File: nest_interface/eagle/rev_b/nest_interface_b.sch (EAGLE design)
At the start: 141 parts, among them J1 MOLEX_MICRO_USB_B_047346, J10 CONN_BLOCK_2, J11 CONN_BLOCK_2, J12 CONN_BLOCK_2, J13 CONN_BLOCK_2, J14 CONN_BLOCK_3, J15 CONN_BLOCK_3, J16 CONN_BLOCK_7, J17 CONN_BLOCK_7, J18 CONN_BLOCK_8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

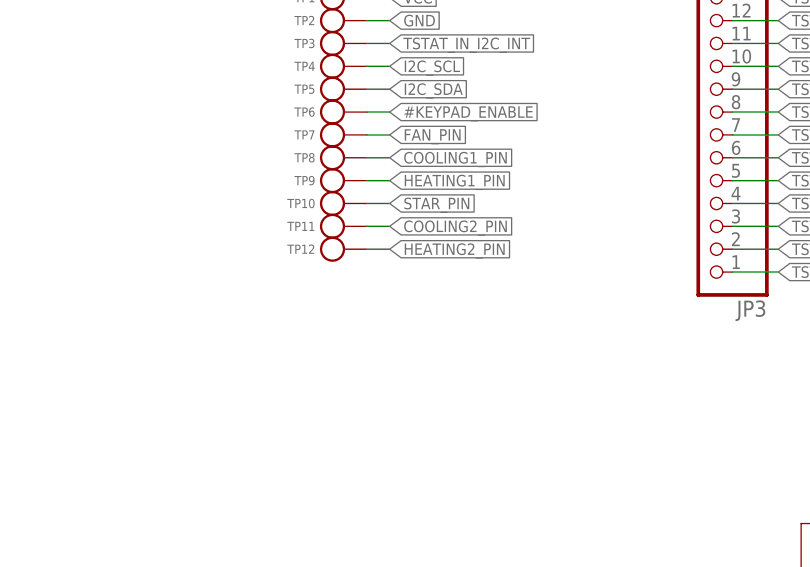
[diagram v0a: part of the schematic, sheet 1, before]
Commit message: moved gpio interrupt to pin2.7
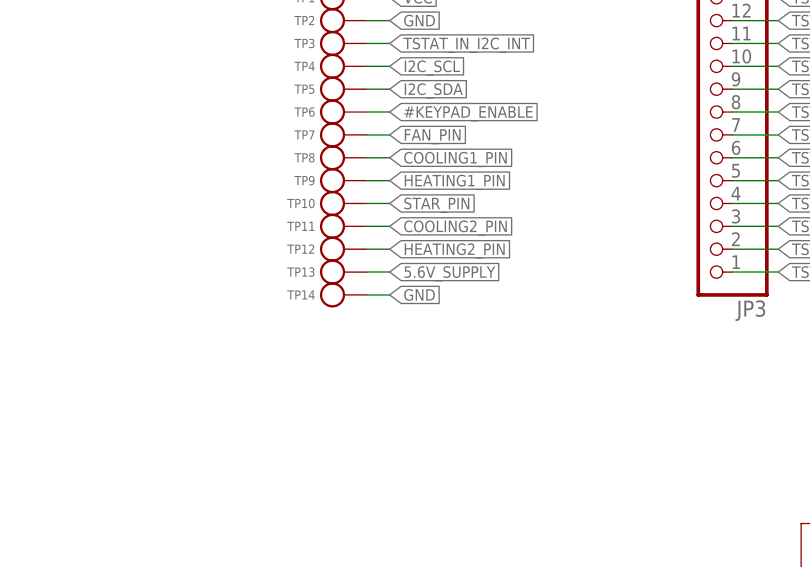
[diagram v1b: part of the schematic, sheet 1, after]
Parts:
- added TP13, TP14: TEST_POINT_0.040IN, nest_interface:TEST_POINT_0.040IN
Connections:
- removed net EPIC_P2.7: J3.3, U1.I2C0/~SPI0
- new net EPIC_P1.2: J3.3, U1.P1.2
- net 5.6V_SUPPLY: now also TP13.TESTPOINT
- net GND: now also TP14.TESTPOINT
- net TSTAT_IN_I2C_INT: now also U1.I2C0/~SPI0; no longer U1.P1.2
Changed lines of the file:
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@@
 <part name="JP2" library="pinhead" deviceset="PINHD-1X14" device=""/>
 <part name="JP3" library="pinhead" deviceset="PINHD-1X14" device=""/>
+<part name="TP13" library="nest_interface" deviceset="TEST_POINT_0.040IN" device="">
+<attribute name="DIGIKEY" value="5001K-ND"/>
+</part>
+<part name="TP14" library="nest_interface" deviceset="TEST_POINT_0.040IN" device="">
+<attribute name="DIGIKEY" value="5001K-ND"/>
+</part>
 </parts>
 <sheets>
@@
 <instance part="TP12" gate="G$1" x="96.52" y="45.72"/>
 <instance part="JP3" gate="A" x="137.16" y="58.42" rot="R180"/>
+<instance part="TP13" gate="G$1" x="96.52" y="43.18"/>
+<instance part="TP14" gate="G$1" x="96.52" y="40.64"/>
 </instances>
 <busses>
@@
 <label x="101.6" y="71.12" size="1.27" layer="95" xref="yes"/>
 </segment>
+<segment>
+<pinref part="TP14" gate="G$1" pin="TESTPOINT"/>
+<wire x1="99.06" y1="40.64" x2="101.6" y2="40.64" width="0.1524" layer="91"/>
+<label x="101.6" y="40.64" size="1.27" layer="95" xref="yes"/>
+</segment>
 </net>
 <net name="VCC" class="0">
@@
 <wire x1="114.3" y1="101.6" x2="111.76" y2="101.6" width="0.1524" layer="91"/>
 <label x="111.76" y="101.6" size="1.27" layer="95" rot="R180" xref="yes"/>
+</segment>
+<segment>
+<pinref part="TP13" gate="G$1" pin="TESTPOINT"/>
+<wire x1="99.06" y1="43.18" x2="101.6" y2="43.18" width="0.1524" layer="91"/>
+<label x="101.6" y="43.18" size="1.27" layer="95" xref="yes"/>
 </segment>
 </net>
@@
 </segment>
 </net>
-<net name="EPIC_P2.7" class="0">
+<net name="HEATING2_PIN" class="0">
+<segment>
+<pinref part="U1" gate="G$1" pin="P2.6"/>
+<wire x1="223.52" y1="119.38" x2="226.06" y2="119.38" width="0.1524" layer="91"/>
+<label x="226.06" y="119.38" size="1.27" layer="95" xref="yes"/>
+</segment>
+</net>
+<net name="COOLING2_PIN" class="0">
+<segment>
+<pinref part="U1" gate="G$1" pin="P2.3"/>
+<wire x1="223.52" y1="116.84" x2="226.06" y2="116.84" width="0.1524" layer="91"/>
+<label x="226.06" y="116.84" size="1.27" layer="95" xref="yes"/>
+</segment>
+</net>
+<net name="STAR_PIN" class="0">
+<segment>
+<pinref part="U1" gate="G$1" pin="P2.1"/>
+<wire x1="223.52" y1="114.3" x2="226.06" y2="114.3" width="0.1524" layer="91"/>
+<label x="226.06" y="114.3" size="1.27" layer="95" xref="yes"/>
+</segment>
+</net>
+<net name="I2C_SCL" class="0">
+<segment>
+<pinref part="U1" gate="G$1" pin="SCLK0/SCL"/>
+<wire x1="190.5" y1="162.56" x2="190.5" y2="177.8" width="0.1524" layer="91"/>
+<wire x1="190.5" y1="177.8" x2="205.74" y2="177.8" width="0.1524" layer="91"/>
+<label x="205.74" y="177.8" size="1.27" layer="95" xref="yes"/>
+</segment>
+<segment>
+<pinref part="J3" gate="A" pin="15"/>
+<wire x1="45.72" y1="144.78" x2="38.1" y2="144.78" width="0.1524" layer="91"/>
+<label x="38.1" y="144.78" size="1.27" layer="95" rot="R180" xref="yes"/>
+</segment>
+</net>
+<net name="I2C_SDA" class="0">
+<segment>
+<pinref part="U1" gate="G$1" pin="MOSI0/SDA"/>
+<wire x1="195.58" y1="162.56" x2="195.58" y2="172.72" width="0.1524" layer="91"/>
+<wire x1="195.58" y1="172.72" x2="205.74" y2="172.72" width="0.1524" layer="91"/>
+<label x="205.74" y="172.72" size="1.27" layer="95" xref="yes"/>
+</segment>
+<segment>
+<pinref part="J3" gate="A" pin="11"/>
+<wire x1="45.72" y1="149.86" x2="38.1" y2="149.86" width="0.1524" layer="91"/>
+<label x="38.1" y="149.86" size="1.27" layer="95" rot="R180" xref="yes"/>
+</segment>
+</net>
+<net name="TSTAT_IN_I2C_INT" class="0">
 <segment>
 <pinref part="U1" gate="G$1" pin="I2C0/~SPI0"/>
@@
 <wire x1="203.2" y1="165.1" x2="205.74" y2="165.1" width="0.1524" layer="91"/>
 <label x="205.74" y="165.1" size="1.27" layer="95" xref="yes"/>
-</segment>
-<segment>
-<pinref part="J3" gate="A" pin="3"/>
-<wire x1="45.72" y1="160.02" x2="38.1" y2="160.02" width="0.1524" layer="91"/>
-<label x="38.1" y="160.02" size="1.27" layer="95" rot="R180" xref="yes"/>
-</segment>
-</net>
-<net name="HEATING2_PIN" class="0">
-<segment>
-<pinref part="U1" gate="G$1" pin="P2.6"/>
-<wire x1="223.52" y1="119.38" x2="226.06" y2="119.38" width="0.1524" layer="91"/>
-<label x="226.06" y="119.38" size="1.27" layer="95" xref="yes"/>
-</segment>
-</net>
-<net name="COOLING2_PIN" class="0">
-<segment>
-<pinref part="U1" gate="G$1" pin="P2.3"/>
-<wire x1="223.52" y1="116.84" x2="226.06" y2="116.84" width="0.1524" layer="91"/>
-<label x="226.06" y="116.84" size="1.27" layer="95" xref="yes"/>
-</segment>
-</net>
-<net name="STAR_PIN" class="0">
-<segment>
-<pinref part="U1" gate="G$1" pin="P2.1"/>
-<wire x1="223.52" y1="114.3" x2="226.06" y2="114.3" width="0.1524" layer="91"/>
-<label x="226.06" y="114.3" size="1.27" layer="95" xref="yes"/>
-</segment>
-</net>
-<net name="I2C_SCL" class="0">
-<segment>
-<pinref part="U1" gate="G$1" pin="SCLK0/SCL"/>
-<wire x1="190.5" y1="162.56" x2="190.5" y2="177.8" width="0.1524" layer="91"/>
-<wire x1="190.5" y1="177.8" x2="205.74" y2="177.8" width="0.1524" layer="91"/>
-<label x="205.74" y="177.8" size="1.27" layer="95" xref="yes"/>
-</segment>
-<segment>
-<pinref part="J3" gate="A" pin="15"/>
-<wire x1="45.72" y1="144.78" x2="38.1" y2="144.78" width="0.1524" layer="91"/>
-<label x="38.1" y="144.78" size="1.27" layer="95" rot="R180" xref="yes"/>
-</segment>
-</net>
-<net name="I2C_SDA" class="0">
-<segment>
-<pinref part="U1" gate="G$1" pin="MOSI0/SDA"/>
-<wire x1="195.58" y1="162.56" x2="195.58" y2="172.72" width="0.1524" layer="91"/>
-<wire x1="195.58" y1="172.72" x2="205.74" y2="172.72" width="0.1524" layer="91"/>
-<label x="205.74" y="172.72" size="1.27" layer="95" xref="yes"/>
-</segment>
-<segment>
-<pinref part="J3" gate="A" pin="11"/>
-<wire x1="45.72" y1="149.86" x2="38.1" y2="149.86" width="0.1524" layer="91"/>
-<label x="38.1" y="149.86" size="1.27" layer="95" rot="R180" xref="yes"/>
-</segment>
-</net>
-<net name="TSTAT_IN_I2C_INT" class="0">
-<segment>
-<pinref part="U1" gate="G$1" pin="P1.2"/>
-<wire x1="195.58" y1="86.36" x2="195.58" y2="53.34" width="0.1524" layer="91"/>
-<wire x1="195.58" y1="53.34" x2="165.1" y2="53.34" width="0.1524" layer="91"/>
-<label x="165.1" y="53.34" size="1.27" layer="95" rot="R180" xref="yes"/>
 </segment>
 </net>
@@
 </segment>
 </net>
+<net name="EPIC_P1.2" class="0">
+<segment>
+<pinref part="U1" gate="G$1" pin="P1.2"/>
+<wire x1="195.58" y1="86.36" x2="195.58" y2="53.34" width="0.1524" layer="91"/>
+<wire x1="195.58" y1="53.34" x2="165.1" y2="53.34" width="0.1524" layer="91"/>
+<label x="165.1" y="53.34" size="1.27" layer="95" rot="R180" xref="yes"/>
+</segment>
+<segment>
+<pinref part="J3" gate="A" pin="3"/>
+<wire x1="45.72" y1="160.02" x2="38.1" y2="160.02" width="0.1524" layer="91"/>
+<label x="38.1" y="160.02" size="1.27" layer="95" rot="R180" xref="yes"/>
+</segment>
+</net>
